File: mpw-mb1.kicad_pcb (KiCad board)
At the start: 2 copper layers, 104.5 x 81 mm, 283 parts, among them J1 Conn_01x06, J10 Conn_01x24, J11 Conn_01x24, J2 Conn_02x02_Odd_Even, J3 613012243121, J4 Conn_01x02, J5 Conn_01x03, J6 UJC-HP-3-SMT-TR, J7 TT03_BREAKOUT, J8 Conn_01x02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

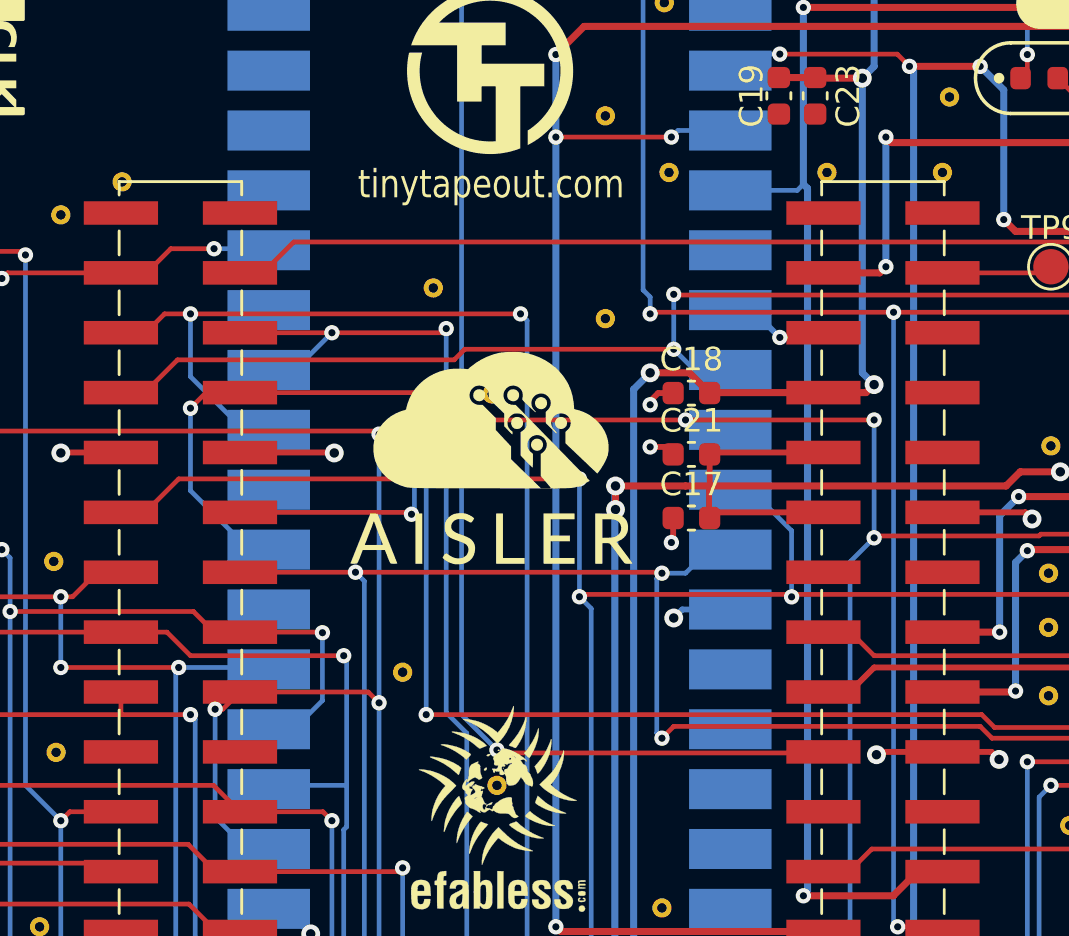
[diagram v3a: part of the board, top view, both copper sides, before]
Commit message: carrier 1 symbol -> 2 placements fix
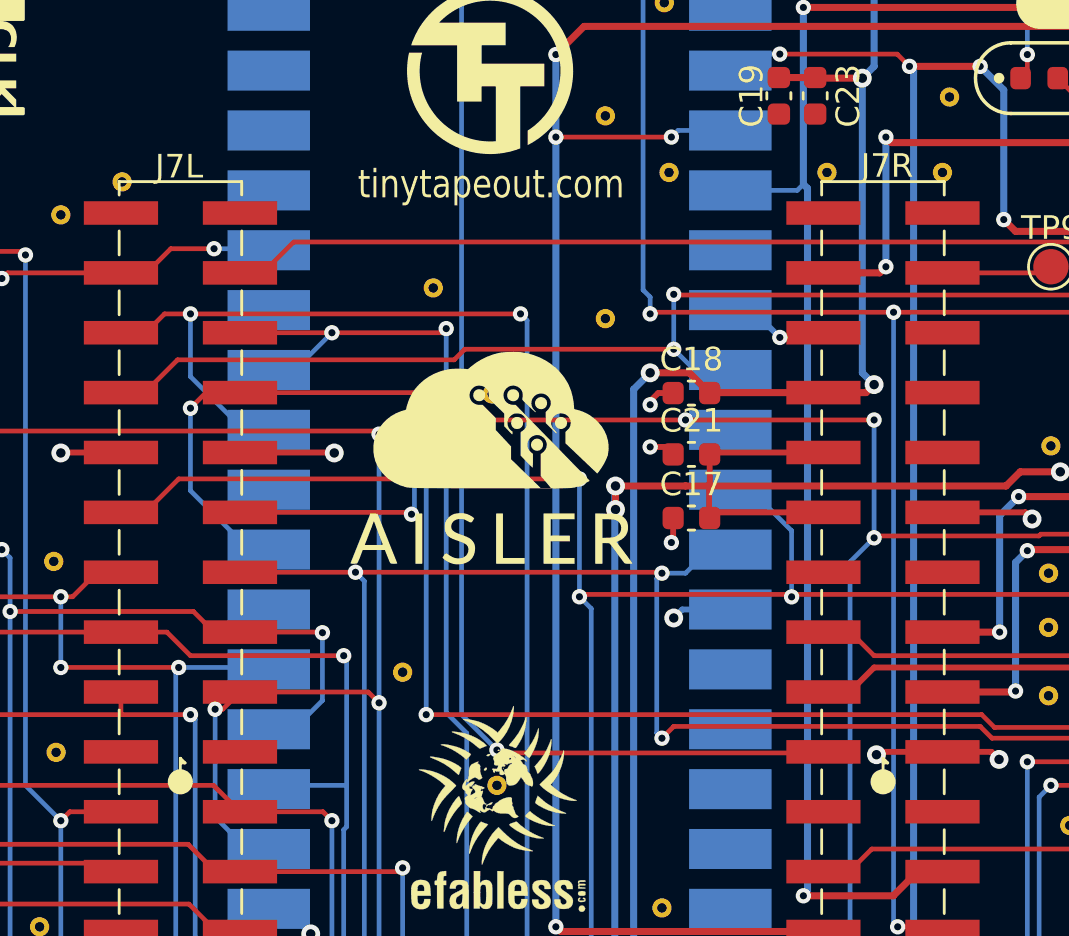
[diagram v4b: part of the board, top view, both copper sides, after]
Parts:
- added J7L: 2x20_P2.54mm_Pinheader, TinyTapeout:TT_BREAKOUT_PINHEADER_PLACEHOLDER, F.Cu at (94.1, 93.3)
- added J7R: 2x20_P2.54mm_Pinheader, TinyTapeout:TT_BREAKOUT_PINHEADER_PLACEHOLDER, F.Cu at (123.9, 93.3)
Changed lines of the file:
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@@
     (pad_to_mask_clearance 0)
     (aux_axis_origin 56.5 134.5)
+    (grid_origin 56.5 134.5)
     (pcbplotparams
       (layerselection 0x00810fc_ffffffff)
@@
       (net 1 "GND") (zone_connect 2))
   )
+  (footprint "TinyTapeout:TT_BREAKOUT_PINHEADER_PLACEHOLDER" (layer "F.Cu")
+    (at 123.88 93.35)
+    (descr "Placeholder for components that need BOM/POS file inclusion")
+    (attr smd board_only)
+    (fp_text reference "J7R" (at 0.17 -26.13 unlocked) (layer "F.SilkS")
+        (effects (font (size 1 1) (thickness 0.15)))
+    )
+    (fp_text value "2x20_P2.54mm_Pinheader" (at 0 1 unlocked) (layer "F.Fab") hide
+        (effects (font (size 1 1) (thickness 0.15)))
+    )
+    (fp_line (start 0 -0.8) (end 0.2 -0.8)
+      (stroke (width 0.12) (type default)) (layer "F.SilkS"))
+    (fp_line (start 0 0) (end 0 -1)
+      (stroke (width 0.12) (type default)) (layer "F.SilkS"))
+    (fp_line (start 0.2 -0.8) (end 0 -1)
+      (stroke (width 0.12) (type default)) (layer "F.SilkS"))
+    (fp_circle (center 0 0) (end 0.223607 0)
+      (stroke (width 0.5) (type default)) (fill none) (layer "F.SilkS"))
+    (fp_circle (center 0 0) (end 0.412311 0)
+      (stroke (width 0.24) (type default)) (fill none) (layer "F.SilkS"))
+  )
   (footprint "Resistor_SMD:R_0603_1608Metric" (layer "F.Cu")
     (at 131.485 56.1 90)
@@
     (property "Sheetname" "")
     (property "ki_description" "Efabless caravel breakout pinout, aisler board")
-    (attr smd)
+    (attr smd exclude_from_pos_files exclude_from_bom)
     (fp_text reference "J7" (at -3.925 2.05 180) (layer "F.SilkS") hide
         (effects (font (size 1 1) (thickness 0.15)))
@@
         (effects (font (size 1 1) (thickness 0.15)))
     )
-    (fp_text user "${REFERENCE}" (at 15.1 0 90) (layer "F.Fab")
+    (fp_text user "${REFERENCE}" (at -14.9 0 90) (layer "F.Fab")
         (effects (font (size 1 1) (thickness 0.15)))
     )
-    (fp_text user "${REFERENCE}" (at -14.9 0 90) (layer "F.Fab")
+    (fp_text user "${REFERENCE}" (at 15.1 0 90) (layer "F.Fab")
         (effects (font (size 1 1) (thickness 0.15)))
     )
@@
     (fp_line (start 17.5 24.89) (end 17.5 25.46)
       (stroke (width 0.12) (type solid)) (layer "F.SilkS"))
+    (fp_circle (center -14.9 0) (end -14.8 0)
+      (stroke (width 0.12) (type default)) (fill none) (layer "F.SilkS"))
+    (fp_circle (center 14.9 0) (end 15 0)
+      (stroke (width 0.12) (type default)) (fill none) (layer "F.SilkS"))
     (fp_line (start -20.8 -25.9) (end -20.8 25.9)
       (stroke (width 0.05) (type solid)) (layer "F.CrtYd"))
@@
     )
   )
+  (footprint "TinyTapeout:TT_BREAKOUT_PINHEADER_PLACEHOLDER" (layer "F.Cu")
+    (at 94.07 93.35)
+    (descr "Placeholder for components that need BOM/POS file inclusion")
+    (attr smd board_only)
+    (fp_text reference "J7L" (at -0.05 -26.1 unlocked) (layer "F.SilkS")
+        (effects (font (size 1 1) (thickness 0.15)))
+    )
+    (fp_text value "2x20_P2.54mm_Pinheader" (at 0 1 unlocked) (layer "F.Fab") hide
+        (effects (font (size 1 1) (thickness 0.15)))
+    )
+    (fp_line (start 0 -0.8) (end 0.2 -0.8)
+      (stroke (width 0.12) (type default)) (layer "F.SilkS"))
+    (fp_line (start 0 0) (end 0 -1)
+      (stroke (width 0.12) (type default)) (layer "F.SilkS"))
+    (fp_line (start 0.2 -0.8) (end 0 -1)
+      (stroke (width 0.12) (type default)) (layer "F.SilkS"))
+    (fp_circle (center 0 0) (end 0.223607 0)
+      (stroke (width 0.5) (type default)) (fill none) (layer "F.SilkS"))
+    (fp_circle (center 0 0) (end 0.412311 0)
+      (stroke (width 0.24) (type default)) (fill none) (layer "F.SilkS"))
+  )
   (footprint "LED_SMD:LED_0603_1608Metric" (layer "F.Cu")
     (at 130.5 63.5)
@@
     )
   )
+  (group "" (id ff7b3de5-614c-4c2a-819b-8a9744864c96)
+    (members
+      2de2d27d-cb06-40ea-8ab3-e2b29fbbafae
+      ce597d91-a78f-48c7-aec6-ddca1db1e698
+      f17855be-c34a-4569-a20f-edc20a68213e
+    )
+  )
